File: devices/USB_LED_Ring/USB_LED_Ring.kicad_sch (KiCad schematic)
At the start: 70 parts, among them J1 JST SH 3 Vert, J2 USB_B_Micro, J3 JST SH 3 Vert, J4 .100, Q1 DMG2305UX, U1 TPS923610, U2 TLV75733PDBV, U3 RP2354A, Y1 ABM8-272-T3

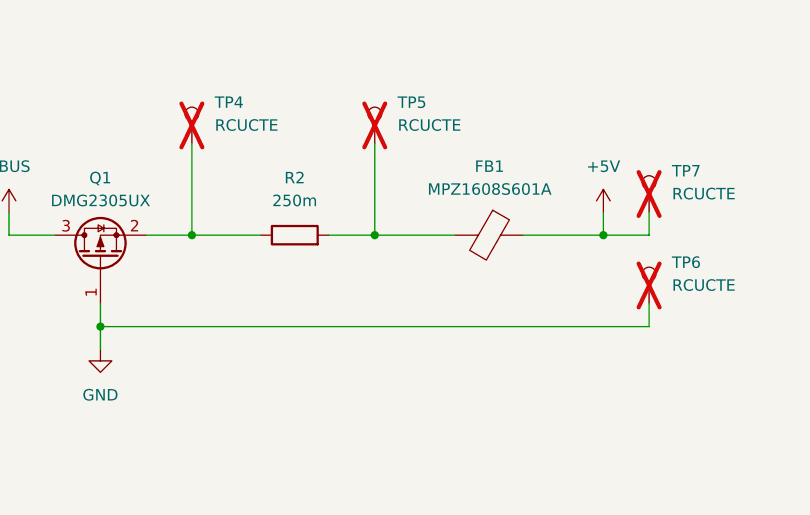
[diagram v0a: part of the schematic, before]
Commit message: Improves the input filter of the LED driver (no self-excitation)
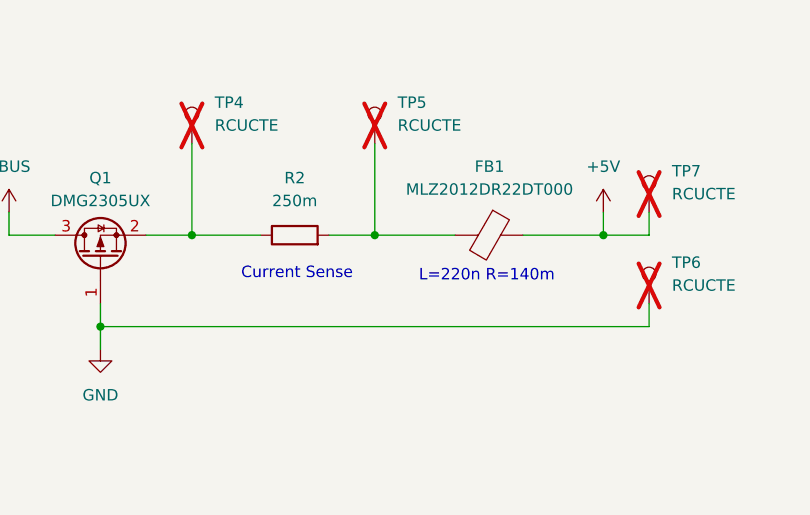
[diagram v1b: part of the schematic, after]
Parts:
- FB1: value MPZ1608S601A -> MLZ2012DR22DT000; footprint Inductor_SMD:L_0603_1608Metric -> Inductor_SMD:L_0805_2012Metric
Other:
- note added: "Current Sense"
- note added: "L=220n R=140m"
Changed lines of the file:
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@@
 		)
 	)
+	(text "Current Sense"
+		(exclude_from_sim no)
+		(at 146.304 42.418 0)
+		(effects
+			(font
+				(size 1.27 1.27)
+			)
+		)
+	)
 	(text "NO Analog, so non filtered AVDD"
 		(exclude_from_sim no)
@@
 		)
 	)
+	(text "L=220n R=140m"
+		(exclude_from_sim no)
+		(at 167.386 42.672 0)
+		(effects
+			(font
+				(size 1.27 1.27)
+			)
+		)
+	)
 	(text "SWD"
 		(exclude_from_sim no)
@@
 			)
 		)
-		(property "Value" "MPZ1608S601A"
+		(property "Value" "MLZ2012DR22DT000"
 			(at 167.6908 33.02 90)
 			(show_name no)
@@
 			)
 		)
-		(property "Footprint" "Inductor_SMD:L_0603_1608Metric"
+		(property "Footprint" "Inductor_SMD:L_0805_2012Metric"
 			(at 167.64 36.322 90)
 			(hide yes)

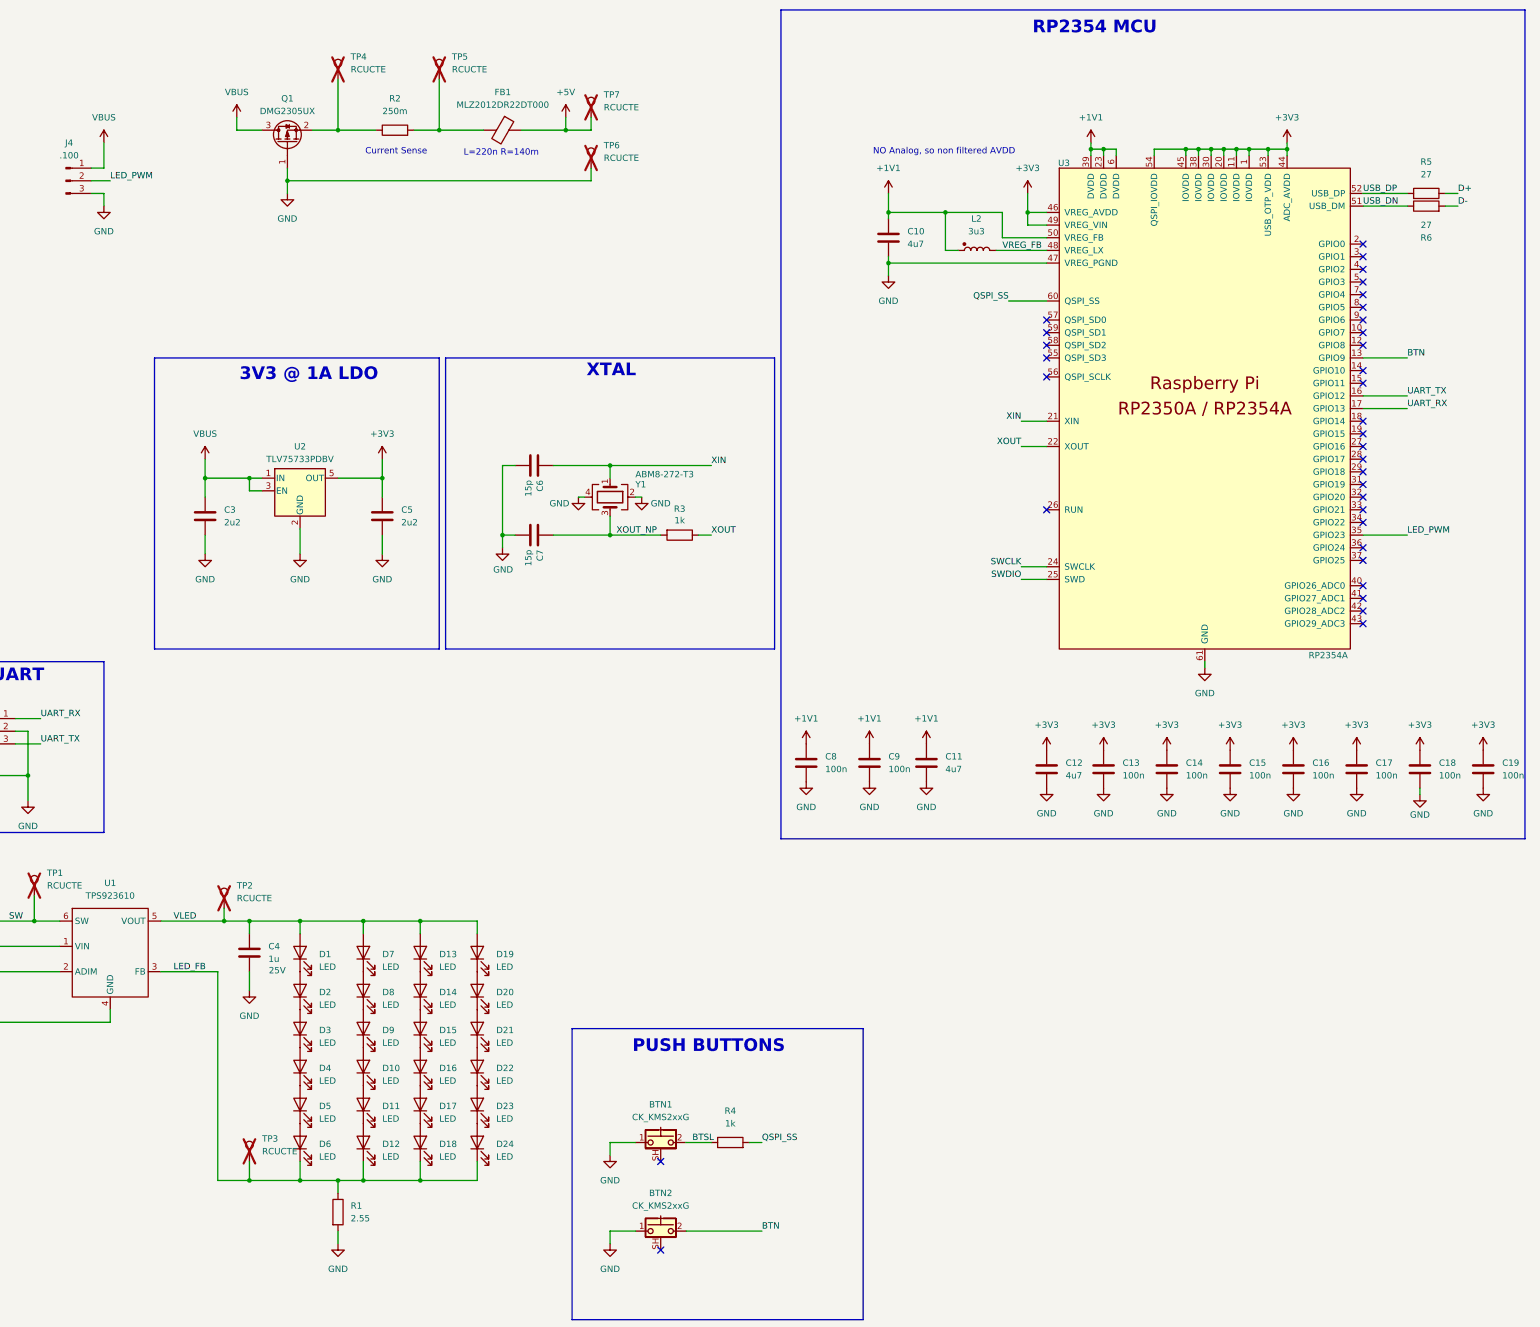
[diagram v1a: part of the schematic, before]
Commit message: Improves input filter for LED driver
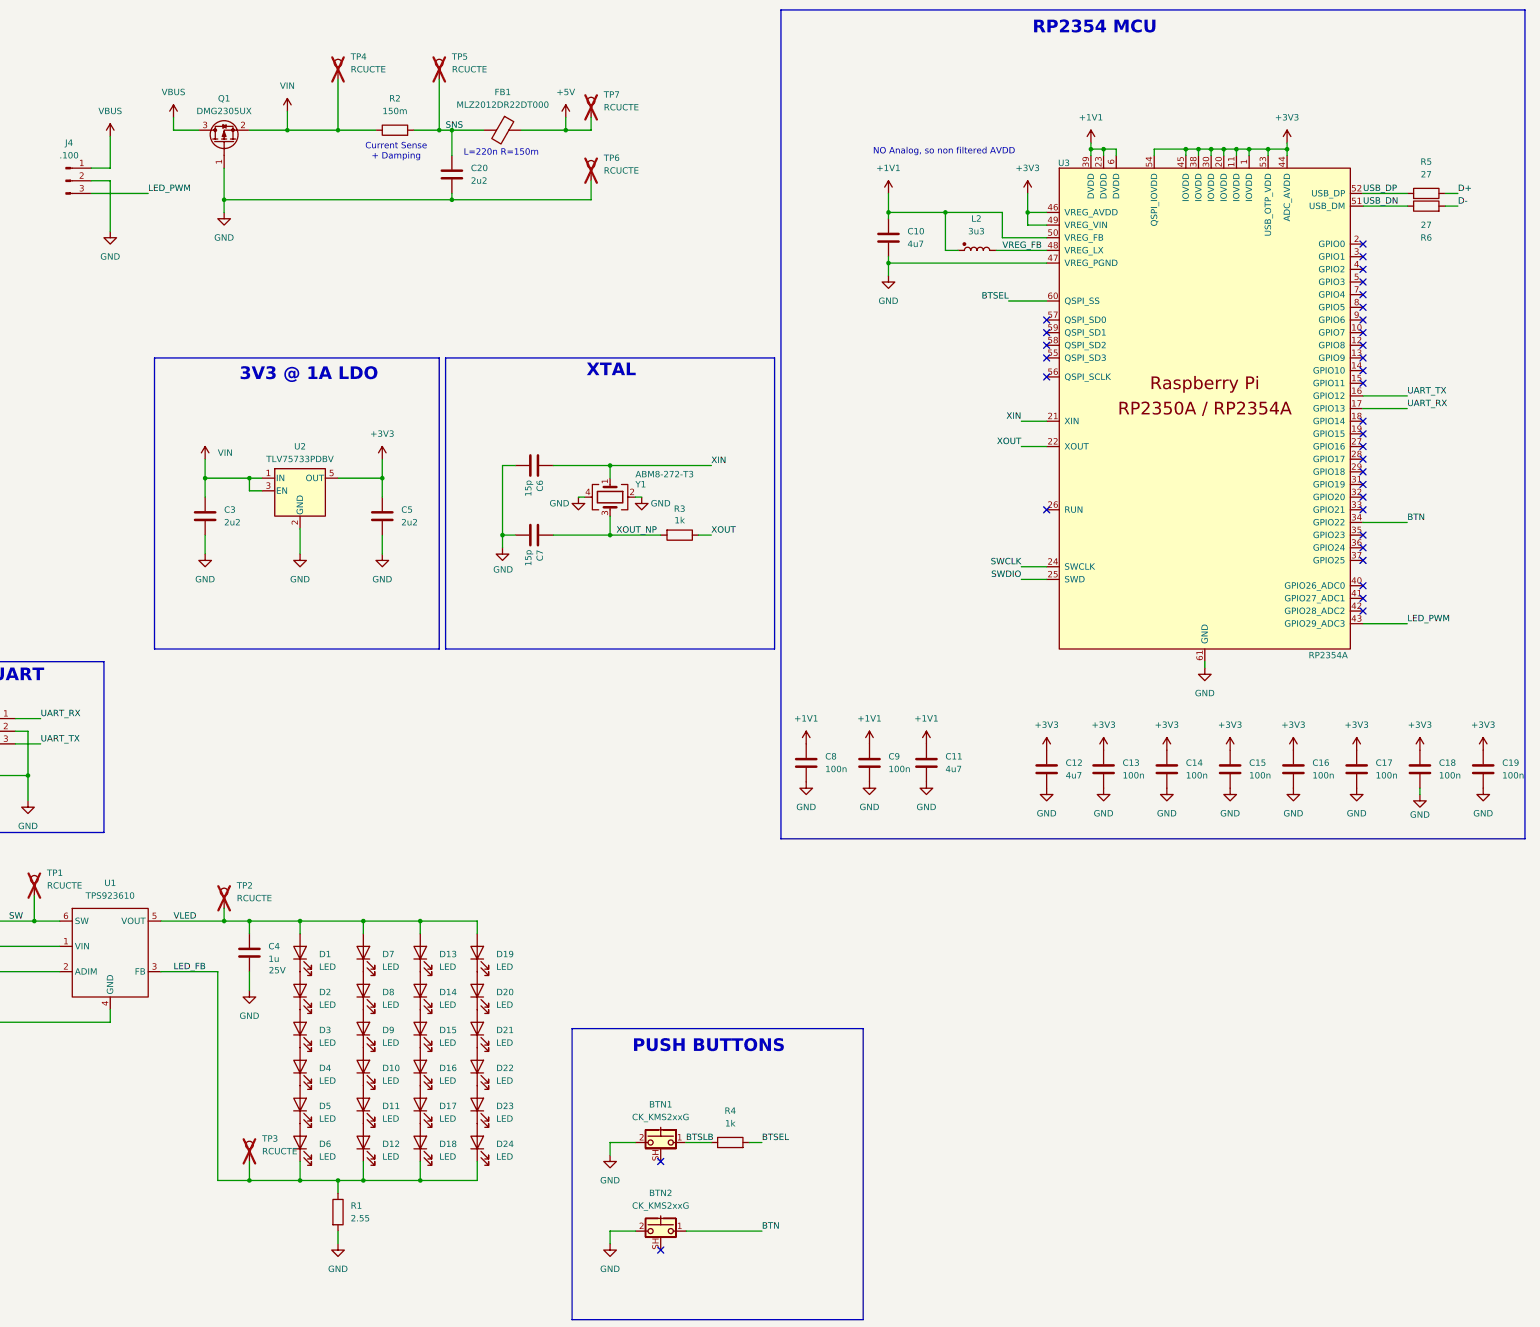
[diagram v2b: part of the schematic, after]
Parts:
- added C20: 2u2, Capacitor_SMD:C_0805_2012Metric, symbol Device:C
- C1, C3, C5: footprint Capacitor_SMD:C_0603_1608Metric -> Capacitor_SMD:C_0805_2012Metric
- J2: footprint Connector_USB:USB_Micro-B_Molex-105017-0001 -> custom:USB_Micro-B_Molex-105017-0001
- R2: value 250m -> 150m
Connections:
- net BTN: now also BTN2.1, U3.34 (GPIO22); no longer BTN2.2, U3.13 (GPIO9)
- net GND: now also BTN1.2, BTN2.2, J4.2 (Pin_2), C20.2; no longer BTN1.1, BTN2.1, J4.3 (Pin_3)
- net LED_PWM: now also J4.3 (Pin_3), U3.43 (GPIO29_ADC3); no longer J4.2 (Pin_2), U3.35 (GPIO23)
- net VBUS: no longer C3.1, U2.1 (IN), U2.3 (EN)
- net SNS: now reaches FB1.2, R2.2, TP5.1
- net SNS: now also C20.1
- net VIN: now reaches Q1.2 (S), R2.1, TP4.1
- net VIN: now also C3.1, U2.1 (IN), U2.3 (EN)
- net BTSL renamed BTSLB
- net BTSLB: now also BTN1.1; no longer BTN1.2
- net QSPI_SS renamed BTSEL
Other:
- note added: "Current Sense + Damping"
- note added: "L=220n R=150m"
- note removed: "Current Sense"
- note removed: "L=220n R=140m"
- moved on the sheet: Q1, TP6

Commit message: !fixup
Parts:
- removed FB1: MLZ2012DR22DT000, Inductor_SMD:L_0805_2012Metric, symbol Device:FerriteBead
- removed Q1: DMG2305UX, Package_TO_SOT_SMD:SOT-23, symbol Transistor_FET:Q_PMOS_GSD
- removed TP7: RCUCTE, custom:RCUCTE, symbol Connector:TestPoint
- added C21: 1n, Capacitor_SMD:C_0402_1005Metric, symbol Device:C
- added L3: 220n, LED_SMD:LED_0805_2012Metric, symbol Device:L
- added R10: 130k, Resistor_SMD:R_0402_1005Metric, symbol Device:R
- added R11, R9: 47k, Resistor_SMD:R_0402_1005Metric, symbol Device:R
- added R7: 6k8, Resistor_SMD:R_0402_1005Metric, symbol Device:R
- added R8: 430k, Resistor_SMD:R_0402_1005Metric, symbol Device:R
- added U4: TPS25947xx, custom:Texas_RPW_VQFN-HR-10_2.1x2.1mm_P0.475mm, symbol custom:TPS25947xx
- C20: value 2u2 -> 4u7
- R2: value 150m -> 100m
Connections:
- net +5V: now also L3.2
- net BTN: now also U3.13 (GPIO9); no longer U3.34 (GPIO22)
- net GND: now also C21.2, R10.1, R7.1, U4.8 (GND)
- net LED_PWM: now also U3.34 (GPIO22); no longer U3.43 (GPIO29_ADC3)
- net SNS: now also L3.1
- net UART_RX: now also U3.3 (GPIO1); no longer U3.17 (GPIO13)
- net UART_TX: now also U3.2 (GPIO0); no longer U3.16 (GPIO12)
- net VBUS: now also R8.2, U4.5 (VIN)
- net VIN: now also R11.2, U4.6 (OUT); no longer U2.3 (EN)
- new net ILIM: R7.2, U4.9 (ILM)
- new net OVLO: R10.2, R9.1, U4.2 (OVLO/OVCSEL)
- new net RUN: R11.1, U2.3 (EN), U4.3 (PG/AUXOFF)
- new net UVLO: R8.1, R9.2, U4.1 (EN/UVLO)
- new net dV: C21.1, U4.7 (dV/dT)
- no-connect marks 35 -> 33
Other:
- note added: ".100 Header"
- note added: "Boost Driver Power Line Isolation"
- note added: "Hot Swap Controller"
- note removed: "L=220n R=150m"
- moved on the sheet: BTN1, BTN2, C1, C10, C11, C12, C13, C14, C15, C16, C17, C18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
